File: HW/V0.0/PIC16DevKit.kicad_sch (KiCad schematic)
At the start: 0 parts

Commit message: PIC16-DevKit-SCH-877 schematic update 1
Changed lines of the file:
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@@
 			(font
 				(face "Consolas")
-				(size 1.27 1.27)
+				(size 1.016 1.016)
 				(thickness 0.254)
-				(bold yes)
 			)
 		)
@@
 			(effects
 				(font
+					(face "Consolas")
 					(size 1.27 1.27)
+					(bold yes)
 				)
 				(justify left bottom)
@@
 			(effects
 				(font
-					(size 1.27 1.27)
+					(face "Consolas")
+					(size 1.016 1.016)
 				)
 				(justify left top)
@@
 			(effects
 				(font
+					(face "Consolas")
 					(size 1.27 1.27)
+					(bold yes)
 				)
 				(justify left bottom)
@@
 			(effects
 				(font
-					(size 1.27 1.27)
+					(face "Consolas")
+					(size 1.016 1.016)
 				)
 				(justify left top)
@@
 			(effects
 				(font
+					(face "Consolas")
 					(size 1.27 1.27)
+					(bold yes)
 				)
 				(justify left bottom)
@@
 			(effects
 				(font
-					(size 1.27 1.27)
+					(face "Consolas")
+					(size 1.016 1.016)
 				)
 				(justify left top)
@@
 			(effects
 				(font
+					(face "Consolas")
 					(size 1.27 1.27)
+					(bold yes)
 				)
 				(justify left bottom)
@@
 			(effects
 				(font
-					(size 1.27 1.27)
+					(face "Consolas")
+					(size 1.016 1.016)
 				)
 				(justify left top)

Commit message: PIC16-DevKit-SCH-877 schematic update 4
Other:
- sheet Power & Peripherals renamed POWER
- sheet Programmer renamed PROGRAMMER
- sheet Target MCU renamed TARGET MCU
- removed sheet AuxiliaryFunctions
- sheet POWER: file Power_Peripherals.kicad_sch -> POWER.kicad_sch
- sheet PROGRAMMER: file Programmer.kicad_sch -> PROGRAMMER.kicad_sch
- sheet TARGET MCU: file Target_MCU.kicad_sch -> TARGET_MCU.kicad_sch
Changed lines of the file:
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@@
 	(text_box "16F877--VDD [4~5.5]\n16F887--VDD [2~5.5]"
 		(exclude_from_sim no)
-		(at 79.375 26.67 0)
-		(size 25.4 6.35)
+		(at 101.6 54.61 0)
+		(size 31.75 6.35)
 		(stroke
 			(width 0.508)
@@
 	)
 	(sheet
-		(at 25.4 63.5)
+		(at 63.5 25.4)
 		(size 25.4 25.4)
 		(fields_autoplaced yes)
@@
 			(color 255 255 194 1.0000)
 		)
-		(property "Sheetname" "Programmer"
-			(at 25.4 62.7376 0)
+		(property "Sheetname" "PROGRAMMER"
+			(at 63.5 24.6376 0)
 			(effects
 				(font
@@
 			)
 		)
-		(property "Sheetfile" "Programmer.kicad_sch"
-			(at 25.4 89.5354 0)
+		(property "Sheetfile" "PROGRAMMER.kicad_sch"
+			(at 63.5 51.4354 0)
 			(effects
 				(font
@@
 	)
 	(sheet
-		(at 76.2 63.5)
+		(at 101.6 25.4)
 		(size 31.75 25.4)
 		(fields_autoplaced yes)
 		(stroke
-			(width 0.381)
+			(width 0.254)
 			(type solid)
 		)
@@
 			(color 255 255 194 1.0000)
 		)
-		(property "Sheetname" "AuxiliaryFunctions"
-			(at 76.2 62.6741 0)
+		(property "Sheetname" "TARGET MCU"
+			(at 101.6 24.6376 0)
 			(effects
 				(font
@@
 			)
 		)
-		(property "Sheetfile" "AuxiliaryFunctions.kicad_sch"
-			(at 76.2 89.5989 0)
-			(effects
-				(font
-					(face "Consolas")
-					(size 1.016 1.016)
-				)
-				(justify left top)
-			)
-		)
-		(instances
-			(project "PIC16DevKit"
-				(path "/17281b91-3f9a-4e36-96b2-66002b412b3a"
-					(page "5")
-				)
-			)
-		)
-	)
-	(sheet
-		(at 76.2 25.4)
-		(size 31.75 25.4)
-		(fields_autoplaced yes)
-		(stroke
-			(width 0.254)
-			(type solid)
-		)
-		(fill
-			(color 255 255 194 1.0000)
-		)
-		(property "Sheetname" "Target MCU"
-			(at 76.2 24.6376 0)
-			(effects
-				(font
-					(face "Consolas")
-					(size 1.27 1.27)
-					(bold yes)
-				)
-				(justify left bottom)
-			)
-		)
-		(property "Sheetfile" "Target_MCU.kicad_sch"
-			(at 76.2 51.4354 0)
+		(property "Sheetfile" "TARGET_MCU.kicad_sch"
+			(at 101.6 51.4354 0)
 			(effects
 				(font
@@
 			(color 255 255 194 1.0000)
 		)
-		(property "Sheetname" "Power & Peripherals"
+		(property "Sheetname" "POWER"
 			(at 25.4 24.6376 0)
 			(effects
@@
 			)
 		)
-		(property "Sheetfile" "Power_Peripherals.kicad_sch"
+		(property "Sheetfile" "POWER.kicad_sch"
 			(at 25.4 51.4354 0)
 			(effects

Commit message: PIC16-DevKit-SCH-877 schematic update 5
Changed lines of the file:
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@@
 				(font
 					(face "Consolas")
-					(size 1.27 1.27)
-					(bold yes)
+					(size 1.016 1.016)
 				)
 				(justify left bottom)
@@
 				(font
 					(face "Consolas")
-					(size 1.27 1.27)
-					(bold yes)
+					(size 1.016 1.016)
 				)
 				(justify left bottom)
@@
 				(font
 					(face "Consolas")
-					(size 1.27 1.27)
-					(bold yes)
+					(size 1.016 1.016)
 				)
 				(justify left bottom)

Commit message: PIC16-DevKit-SCH-877 schematic update 6
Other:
- sheet POWER ports: added USB_N, USB_P, VBUS_SEN, VPP_EN, ~{VTG_EN}; removed none
- sheet PROGRAMMER ports: added CS, LED_BUSY, LED_TGRDY, PG_PGC, PG_PGD, RXD, SCK, SCL, SDA, SDI, SDO, TG_SCL, TG_SDA, TXD, URX, USB_N, USB_P, USB_VBUS, VPP_EN, ~{BT_MODE}, ~{PG_MCLR}, ~{TG_MCLR}, ~{TG_PGC}, ~{TG_PGD}, ~{TG_RXD}, ~{TG_TXD}, ~{VTG_EN}; removed none
- sheet TARGET MCU ports: added AN0, AN1, AN2, AN3, AN4, AN5, INT0, INT1, INT2, PGC, PGD, PWM1, PWM2, RD0, RD1, RD2, RD3, RD4, RD5, RD6, RD7, RXD, SCL, SCLK, SDA, SDI, SDO, T0CKI, T1CKI, TXD, ULED, ~{CS}, ~{MCLR}, ~{UBT}; removed none

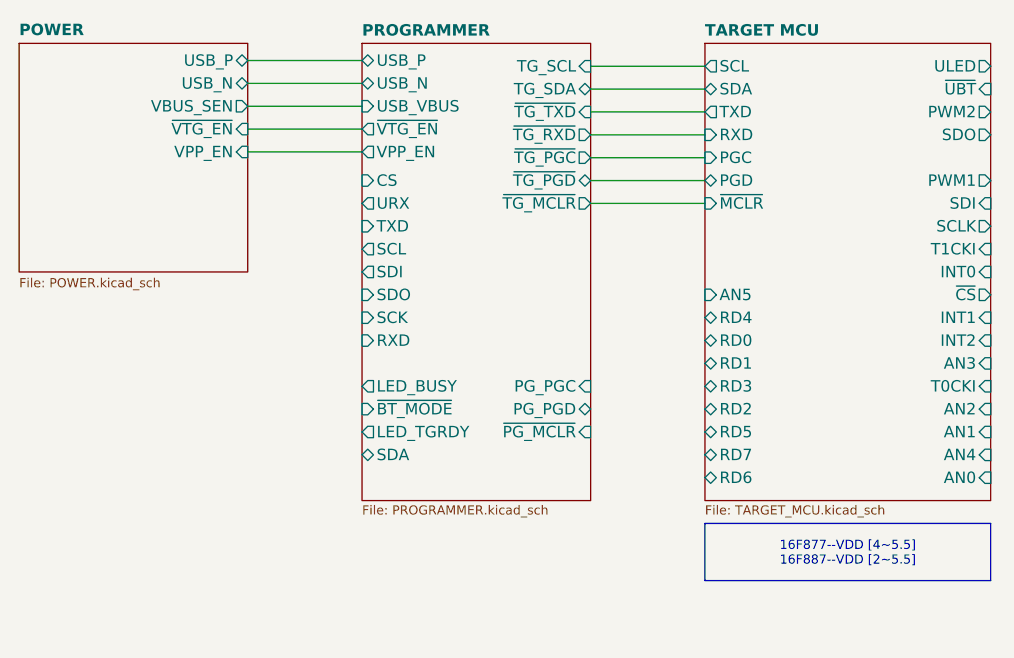
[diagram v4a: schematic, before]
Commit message: PIC16-DevKit-SCH-877 schematic update 7
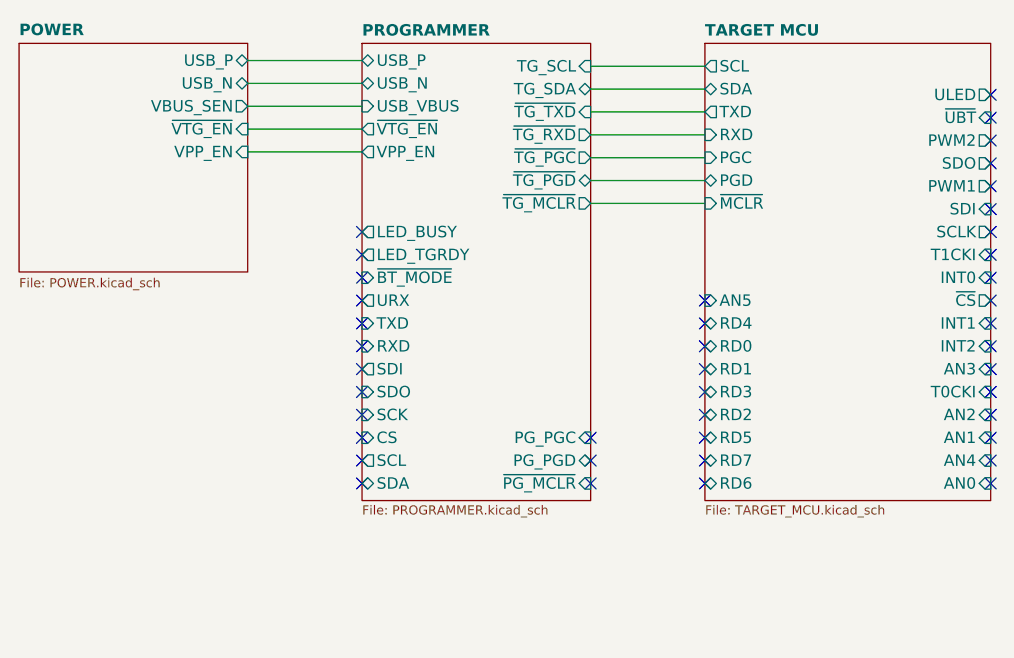
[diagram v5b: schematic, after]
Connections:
- no-connect marks 0 -> 42
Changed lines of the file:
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@@
 	(generator_version "8.0")
 	(paper "A4")
+	(no_connect
+		(at 101.6 71.755)
+	)
+	(no_connect
+		(at 101.6 56.515)
+	)
+	(no_connect
+		(at 133.35 74.295)
+	)
+	(no_connect
+		(at 63.5 61.595)
+	)
+	(no_connect
+		(at 63.5 69.215)
+	)
+	(no_connect
+		(at 63.5 74.295)
+	)
+	(no_connect
+		(at 63.5 71.755)
+	)
+	(no_connect
+		(at 133.35 41.275)
+	)
+	(no_connect
+		(at 88.9 69.215)
+	)
+	(no_connect
+		(at 133.35 53.975)
+	)
+	(no_connect
+		(at 63.5 64.135)
+	)
+	(no_connect
+		(at 63.5 48.895)
+	)
+	(no_connect
+		(at 101.6 61.595)
+	)
+	(no_connect
+		(at 133.35 48.895)
+	)
+	(no_connect
+		(at 133.35 36.195)
+	)
+	(no_connect
+		(at 63.5 51.435)
+	)
+	(no_connect
+		(at 101.6 53.975)
+	)
+	(no_connect
+		(at 63.5 46.355)
+	)
+	(no_connect
+		(at 133.35 31.115)
+	)
+	(no_connect
+		(at 63.5 66.675)
+	)
+	(no_connect
+		(at 63.5 53.975)
+	)
+	(no_connect
+		(at 133.35 61.595)
+	)
+	(no_connect
+		(at 133.35 51.435)
+	)
+	(no_connect
+		(at 101.6 66.675)
+	)
+	(no_connect
+		(at 88.9 71.755)
+	)
+	(no_connect
+		(at 133.35 69.215)
+	)
+	(no_connect
+		(at 133.35 33.655)
+	)
+	(no_connect
+		(at 133.35 38.735)
+	)
+	(no_connect
+		(at 63.5 56.515)
+	)
+	(no_connect
+		(at 88.9 74.295)
+	)
+	(no_connect
+		(at 133.35 43.815)
+	)
+	(no_connect
+		(at 133.35 59.055)
+	)
+	(no_connect
+		(at 101.6 69.215)
+	)
+	(no_connect
+		(at 133.35 56.515)
+	)
+	(no_connect
+		(at 101.6 64.135)
+	)
+	(no_connect
+		(at 101.6 74.295)
+	)
+	(no_connect
+		(at 63.5 59.055)
+	)
+	(no_connect
+		(at 101.6 59.055)
+	)
+	(no_connect
+		(at 133.35 71.755)
+	)
+	(no_connect
+		(at 133.35 46.355)
+	)
+	(no_connect
+		(at 133.35 64.135)
+	)
+	(no_connect
+		(at 133.35 66.675)
+	)
 	(wire
 		(pts
@@
 			(width 0)
 			(type default)
-		)
-	)
-	(text_box "16F877--VDD [4~5.5]\n16F887--VDD [2~5.5]"
-		(exclude_from_sim no)
-		(at 101.6 78.74 0)
-		(size 31.75 6.35)
-		(stroke
-			(width 0)
-			(type default)
-		)
-		(fill
-			(type none)
-		)
-		(effects
-			(font
-				(face "Consolas")
-				(size 1.016 1.016)
-				(thickness 0.254)
-			)
 		)
 	)
@@
 		)
 		(pin "SCL" output
-			(at 63.5 48.26 180)
+			(at 63.5 71.755 180)
 			(effects
 				(font
@@
 		)
 		(pin "TXD" input
-			(at 63.5 45.72 180)
+			(at 63.5 56.515 180)
 			(effects
 				(font
@@
 		)
 		(pin "URX" output
-			(at 63.5 43.18 180)
+			(at 63.5 53.975 180)
 			(effects
 				(font
@@
 		)
 		(pin "CS" input
-			(at 63.5 40.64 180)
+			(at 63.5 69.215 180)
 			(effects
 				(font
@@
 		)
 		(pin "SDA" bidirectional
-			(at 63.5 71.12 180)
+			(at 63.5 74.295 180)
 			(effects
 				(font
@@
 		)
 		(pin "SDI" output
-			(at 63.5 50.8 180)
+			(at 63.5 61.595 180)
 			(effects
 				(font
@@
 		)
 		(pin "SDO" input
-			(at 63.5 53.34 180)
+			(at 63.5 64.135 180)
 			(effects
 				(font
@@
 		)
 		(pin "SCK" input
-			(at 63.5 55.88 180)
+			(at 63.5 66.675 180)
 			(effects
 				(font
@@
 		)
 		(pin "RXD" input
-			(at 63.5 58.42 180)
+			(at 63.5 59.055 180)
 			(effects
 				(font
@@
 		)
 		(pin "PG_PGC" input
-			(at 88.9 63.5 0)
+			(at 88.9 69.215 0)
 			(effects
 				(font
@@
 		)
 		(pin "PG_PGD" bidirectional
-			(at 88.9 66.04 0)
+			(at 88.9 71.755 0)
 			(effects
 				(font
@@
 		)
 		(pin "LED_BUSY" output
-			(at 63.5 63.5 180)
+			(at 63.5 46.355 180)
 			(effects
 				(font
@@
 		)
 		(pin "~{BT_MODE}" input
-			(at 63.5 66.04 180)
+			(at 63.5 51.435 180)
 			(effects
 				(font
@@
 		)
 		(pin "~{PG_MCLR}" input
-			(at 88.9 68.58 0)
+			(at 88.9 74.295 0)
 			(effects
 				(font
@@
 		)
 		(pin "LED_TGRDY" output
-			(at 63.5 68.58 180)
+			(at 63.5 48.895 180)
 			(effects
 				(font
@@
 		)
 		(pin "ULED" output
-			(at 133.35 27.94 0)
+			(at 133.35 31.115 0)
 			(effects
 				(font
@@
 		)
 		(pin "~{UBT}" input
-			(at 133.35 30.48 0)
+			(at 133.35 33.655 0)
 			(effects
 				(font
@@
 		)
 		(pin "PWM2" output
-			(at 133.35 33.02 0)
+			(at 133.35 36.195 0)
 			(effects
 				(font
@@
 		)
 		(pin "SDO" output
-			(at 133.35 35.56 0)
+			(at 133.35 38.735 0)
 			(effects
 				(font
@@
 		)
 		(pin "PWM1" output
-			(at 133.35 40.64 0)
+			(at 133.35 41.275 0)
 			(effects
 				(font
@@
 		)
 		(pin "SDI" input
-			(at 133.35 43.18 0)
+			(at 133.35 43.815 0)
 			(effects
 				(font
@@
 		)
 		(pin "SCLK" output
-			(at 133.35 45.72 0)
+			(at 133.35 46.355 0)
 			(effects
 				(font
@@
 		)
 		(pin "T1CKI" input
-			(at 133.35 48.26 0)
+			(at 133.35 48.895 0)
 			(effects
 				(font
@@
 		)
 		(pin "INT0" input
-			(at 133.35 50.8 0)
+			(at 133.35 51.435 0)
 			(effects
 				(font
@@
 		)
 		(pin "~{CS}" output
-			(at 133.35 53.34 0)
+			(at 133.35 53.975 0)
 			(effects
 				(font
@@
 		)
 		(pin "INT1" input
-			(at 133.35 55.88 0)
+			(at 133.35 56.515 0)
 			(effects
 				(font
@@
 		)
 		(pin "INT2" input
-			(at 133.35 58.42 0)
+			(at 133.35 59.055 0)
 			(effects
 				(font
@@
 		)
 		(pin "AN3" input
-			(at 133.35 60.96 0)
+			(at 133.35 61.595 0)
 			(effects
 				(font
@@
 		)
 		(pin "T0CKI" input
-			(at 133.35 63.5 0)
+			(at 133.35 64.135 0)
 			(effects
 				(font
@@
 		)
 		(pin "AN2" input
-			(at 133.35 66.04 0)
+			(at 133.35 66.675 0)
 			(effects
 				(font
@@
 		)
 		(pin "AN1" input
-			(at 133.35 68.58 0)
+			(at 133.35 69.215 0)
 			(effects
 				(font
@@
 		)
 		(pin "AN4" input
-			(at 133.35 71.12 0)
+			(at 133.35 71.755 0)
 			(effects
 				(font
@@
 		)
 		(pin "AN0" input
-			(at 133.35 73.66 0)
+			(at 133.35 74.295 0)
 			(effects
 				(font
@@
 		)
 		(pin "RD6" bidirectional
-			(at 101.6 73.66 180)
+			(at 101.6 74.295 180)
 			(effects
 				(font
@@
 		)
 		(pin "RD7" bidirectional
-			(at 101.6 71.12 180)
+			(at 101.6 71.755 180)
 			(effects
 				(font
@@
 		)
 		(pin "RD5" bidirectional
-			(at 101.6 68.58 180)
+			(at 101.6 69.215 180)
 			(effects
 				(font
@@
 		)
 		(pin "RD2" bidirectional
-			(at 101.6 66.04 180)
+			(at 101.6 66.675 180)
 			(effects
 				(font
@@
 		)
 		(pin "RD3" bidirectional
-			(at 101.6 63.5 180)
+			(at 101.6 64.135 180)
 			(effects
 				(font
@@
 		)
 		(pin "RD1" bidirectional
-			(at 101.6 60.96 180)
+			(at 101.6 61.595 180)
 			(effects
 				(font
@@
 		)
 		(pin "RD0" bidirectional
-			(at 101.6 58.42 180)
+			(at 101.6 59.055 180)
 			(effects
 				(font
@@
 		)
 		(pin "RD4" bidirectional
-			(at 101.6 55.88 180)
+			(at 101.6 56.515 180)
 			(effects
 				(font
@@
 		)
 		(pin "AN5" input
-			(at 101.6 53.34 180)
-			(effects
-				(font
+			(at 101.6 53.975 180)
+			(effects
+				(font

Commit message: PIC16-DevKit-PCB-877 layout update 2
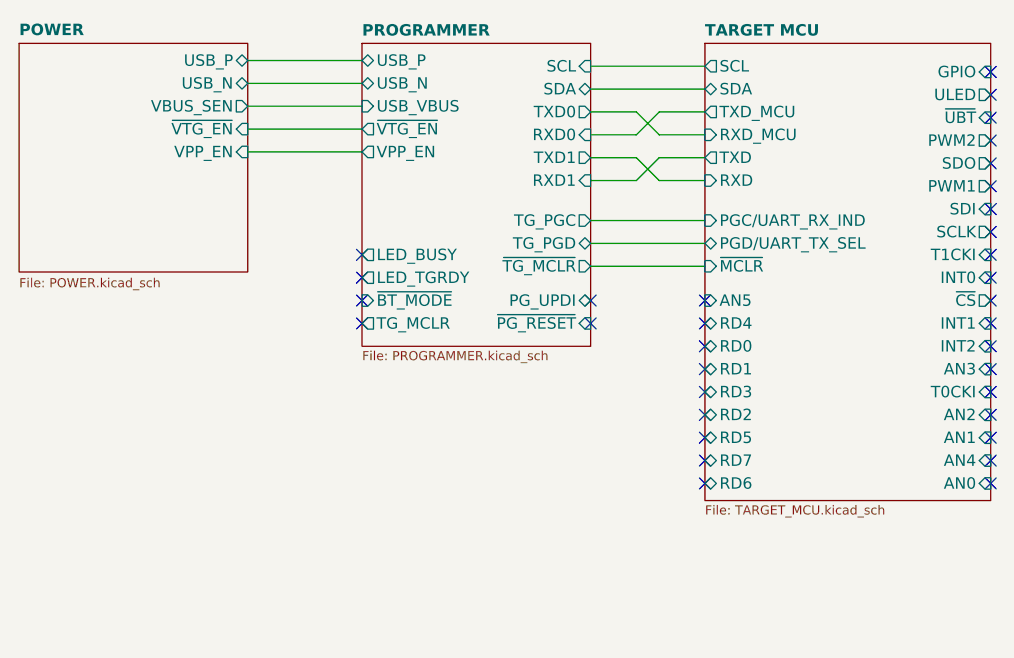
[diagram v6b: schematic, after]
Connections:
- no-connect marks 42 -> 34
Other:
- sheet PROGRAMMER ports: added PG_UPDI, RXD0, RXD1, TG_MCLR, TG_PGC, TG_PGD, TXD0, TXD1, ~{PG_RESET}; removed CS, PG_PGC, PG_PGD, RXD, SCK, SDI, SDO, TG_SCL, TG_SDA, TXD, URX, ~{PG_MCLR}, ~{TG_PGC}, ~{TG_PGD}, ~{TG_RXD}, ~{TG_TXD}
- sheet TARGET MCU ports: added GPIO, PGC/UART_RX_IND, PGD/UART_TX_SEL, RXD_MCU, TXD_MCU; removed PGC, PGD
